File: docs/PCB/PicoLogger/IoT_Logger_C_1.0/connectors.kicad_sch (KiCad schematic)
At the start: 8 parts, among them J3 USB-C, J4 Sensor, J5 LCD 16x2, J6 Additional, J7 SPI, J8 Relay, U5 TPD2EUSB30

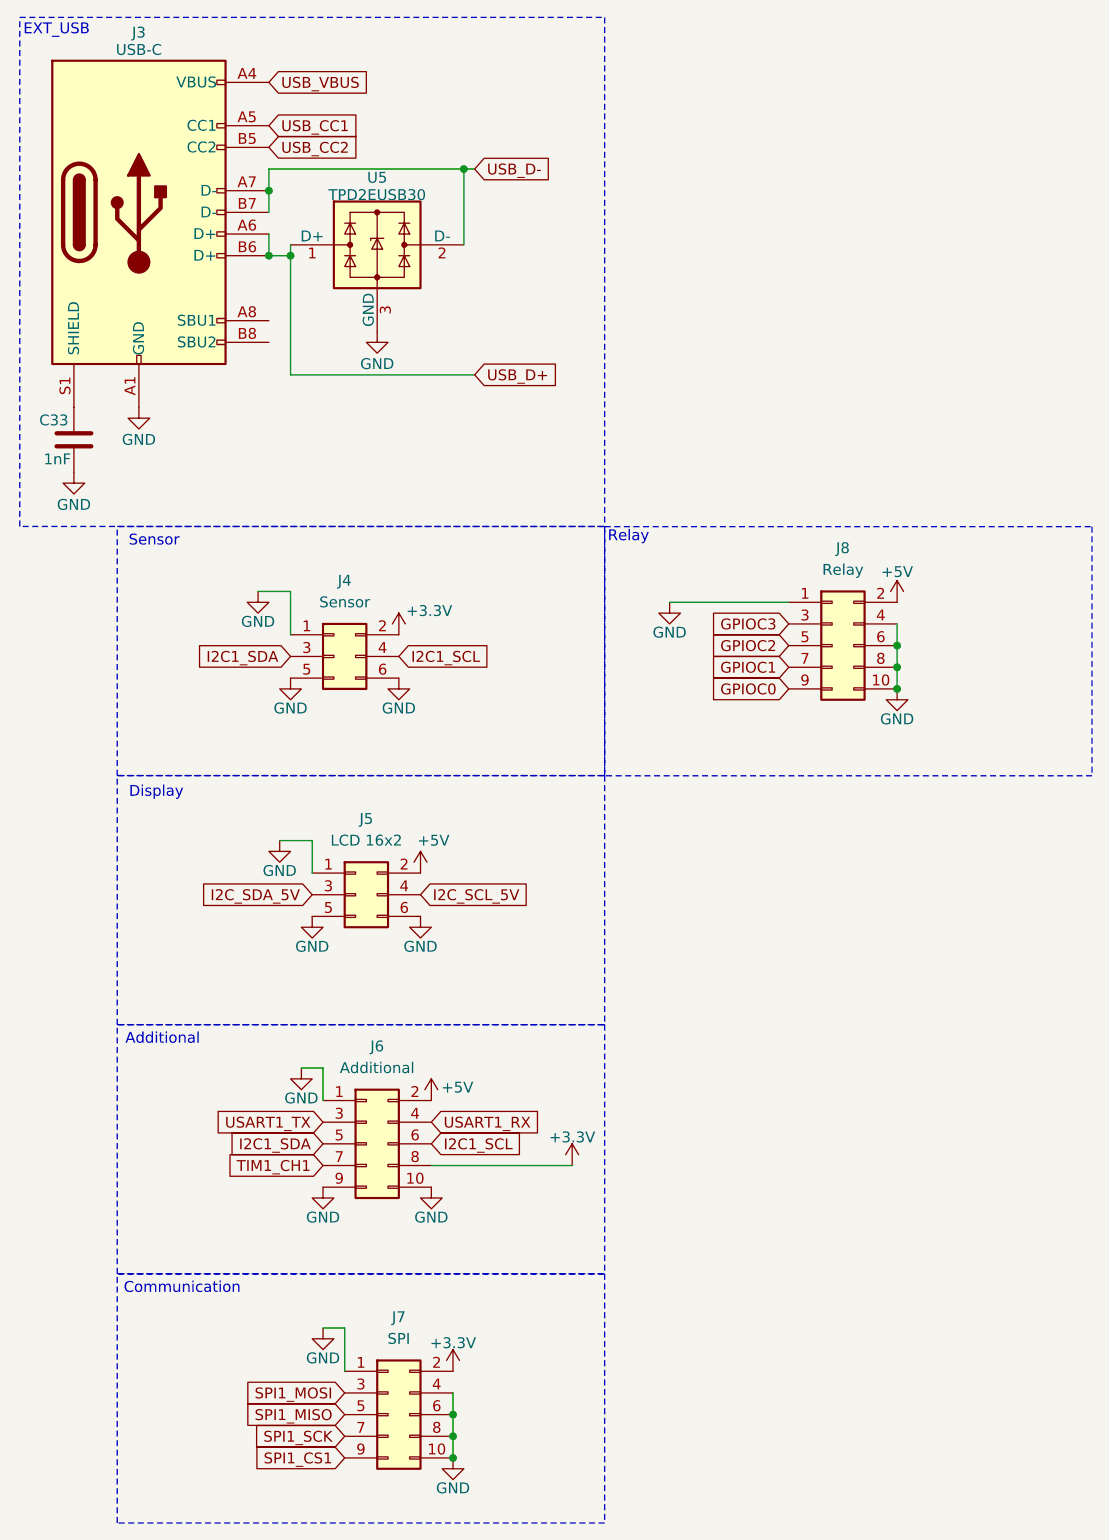
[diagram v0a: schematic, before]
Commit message: Logger IoT B and C production files generated, backend and frontend prepared for new logger type.
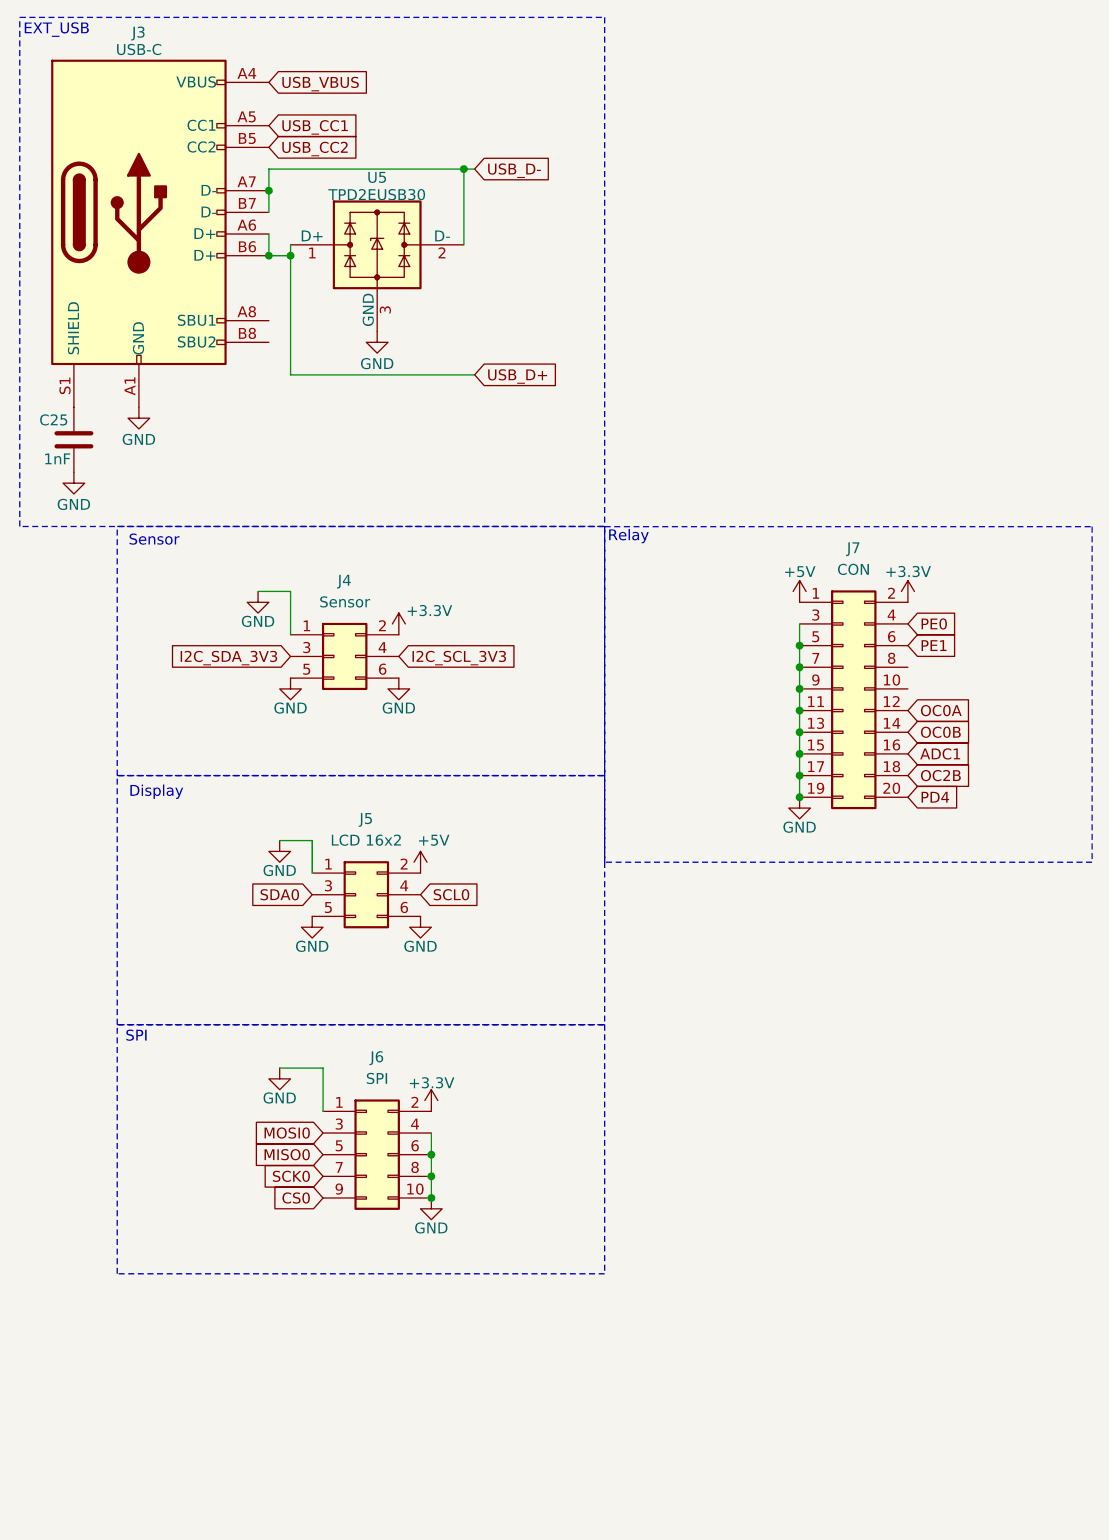
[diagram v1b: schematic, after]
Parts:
- removed J6: Additional, Connector_IDC:IDC-Header_2x05_P2.54mm_Vertical, symbol Connector_Generic:Conn_02x05_Odd_Even
- removed J8: Relay, Connector_IDC:IDC-Header_2x05_P2.54mm_Vertical, symbol Connector_Generic:Conn_02x05_Odd_Even
- added J7: CON, Connector_PinSocket_2.54mm:PinSocket_2x10_P2.54mm_Vertical, symbol Connector_Generic:Conn_02x10_Odd_Even
- renumbered C33 to C25, J7 to J6
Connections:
- net +3.3V: now also J7.2 (Pin_2)
- net +5V: now also J7.1 (Pin_1)
- net GND: now also J7.11 (Pin_11), J7.13 (Pin_13), J7.15 (Pin_15), J7.17 (Pin_17), J7.19 (Pin_19), J7.3 (Pin_3), J7.5 (Pin_5), J7.7 (Pin_7), J7.9 (Pin_9)
- net I2C1_SCL renamed I2C_SCL_3V3
- net I2C1_SDA renamed I2C_SDA_3V3
- net I2C_SCL_5V renamed SCL0
- net I2C_SDA_5V renamed SDA0
- net SPI1_CS1 renamed CS0
- net SPI1_MISO renamed MISO0
- net SPI1_MOSI renamed MOSI0
- net SPI1_SCK renamed SCK0
- new net ADC1: J7.16 (Pin_16)
- new net OC0A: J7.12 (Pin_12)
- new net OC0B: J7.14 (Pin_14)
- new net OC2B: J7.18 (Pin_18)
- new net PD4: J7.20 (Pin_20)
- new net PE0: J7.4 (Pin_4)
- new net PE1: J7.6 (Pin_6)
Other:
- note added: "SPI"
- note removed: "Additional"
- note removed: "Communication"
- title: IoT Logger A - Connectors -> IoT Logger C - Connectors
- moved on the sheet: J6
